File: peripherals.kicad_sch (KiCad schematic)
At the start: 63 parts, among them SW1 USER, SW2 BOOTSEL, SW3 RESET, U2 ATECC608A-MAHDA, U3 W25Q128XXX

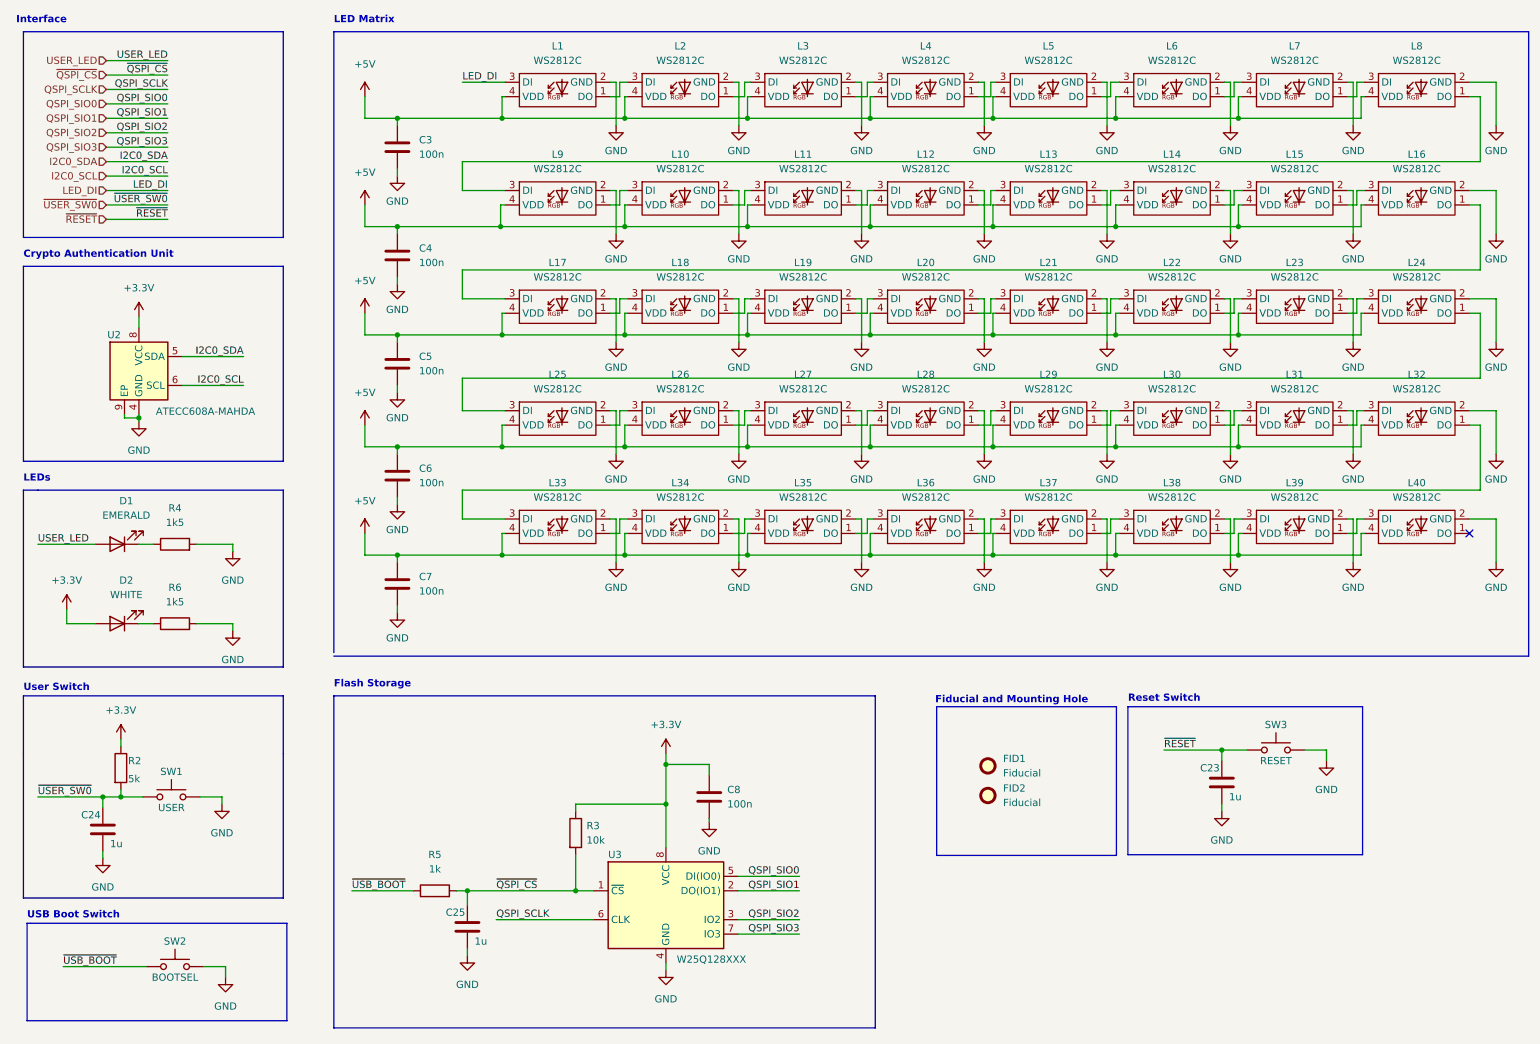
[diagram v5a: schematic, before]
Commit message: Remove trace under usb trace
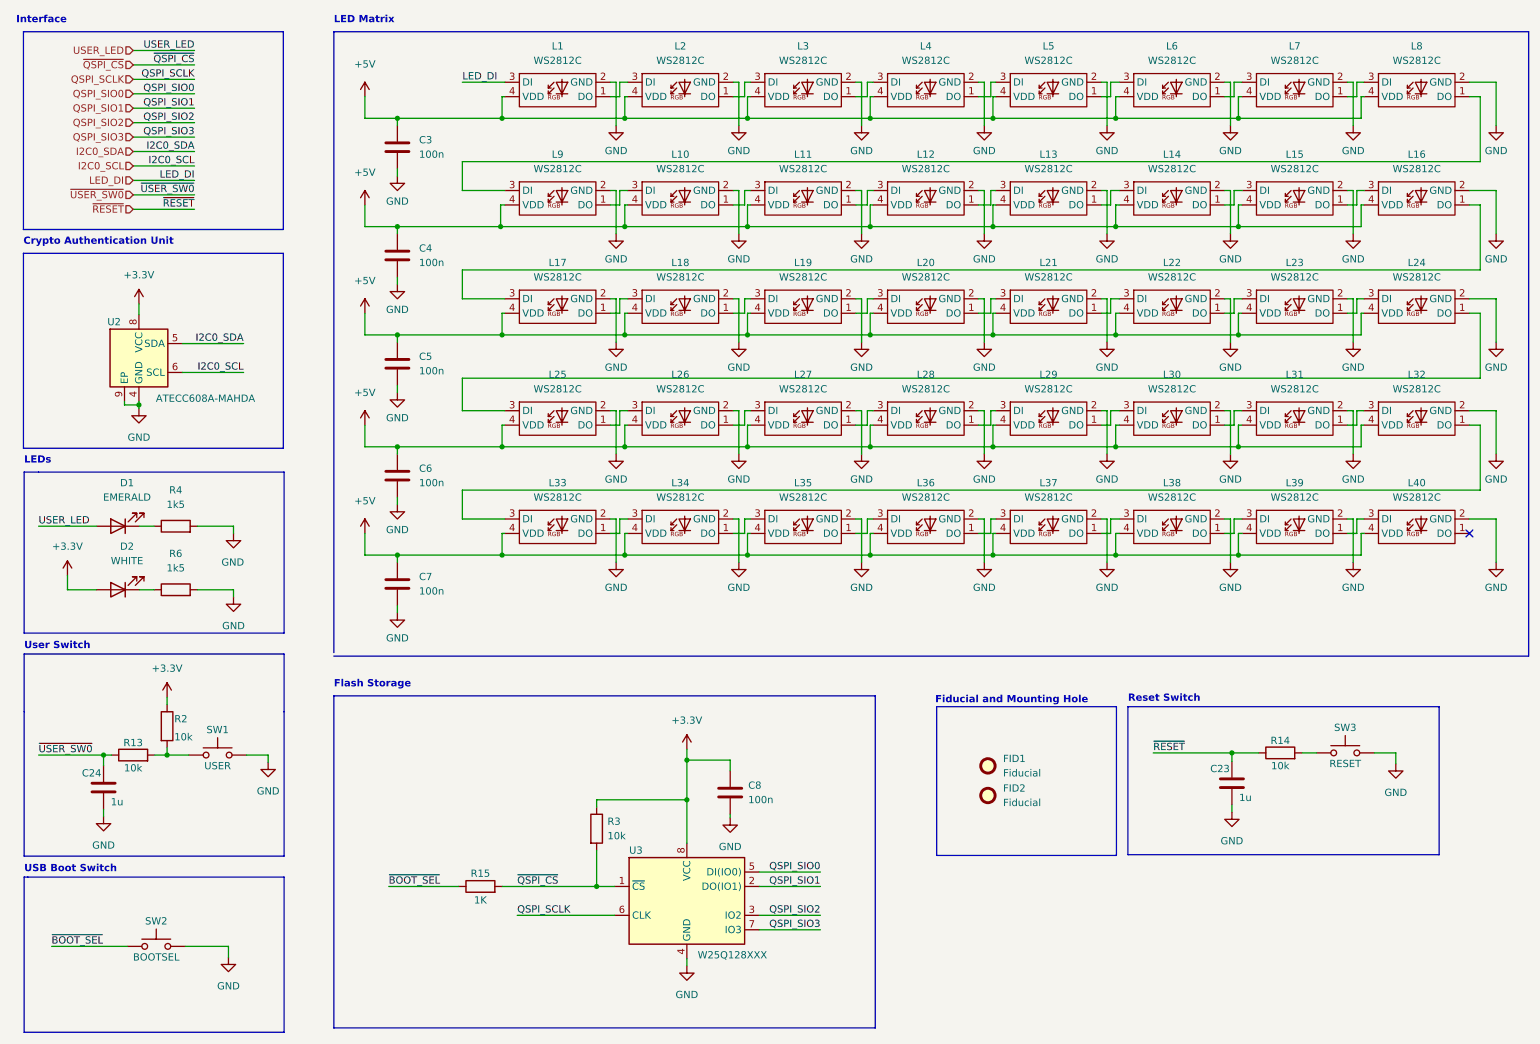
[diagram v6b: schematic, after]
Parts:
- removed C25: 1u, Capacitor_SMD:C_0402_1005Metric, symbol Device:C
- removed R5: 1k, Resistor_SMD:R_0402_1005Metric, symbol Device:R
- added R13, R14: 10k, Resistor_SMD:R_0402_1005Metric, symbol Device:R
- added R15: 1K, Resistor_SMD:R_0402_1005Metric, symbol Device:R
- R2: value 5k -> 10k
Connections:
- net ~{QSPI_CS}: now also R15.2
- net ~{RESET}: now also R14.1; no longer SW3.1
- net ~{USER_SW0}: now also R13.1; no longer R2.2, SW1.1
- net ~{USB_BOOT} renamed ~{BOOT_SEL}
- net ~{BOOT_SEL}: now also R15.1
- new net: R13.2, R2.2, SW1.1
- new net: R14.2, SW3.1
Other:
- moved on the sheet: C23, C24, C8, D1, D2, R2, R3, R4, R6, SW1, SW2, SW3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

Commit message: Production Design V1.0
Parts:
- added R16, R5: 4.7k, Resistor_SMD:R_0402_1005Metric, symbol Device:R
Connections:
- net +3V3: now also R16.1, R5.1
- net I2C0_SCL: now also R16.2
- net I2C0_SDA: now also R5.2
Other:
- moved on the sheet: U2

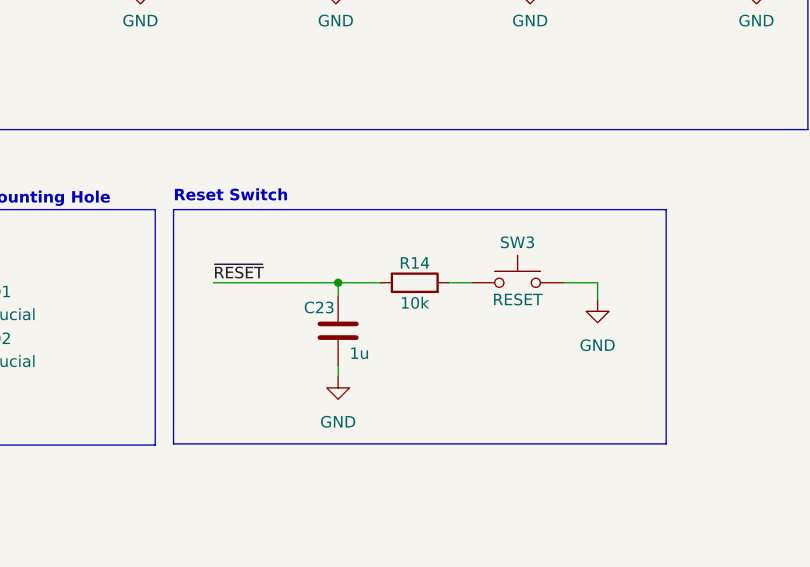
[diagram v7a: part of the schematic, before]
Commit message: Fix issues found on production prototype
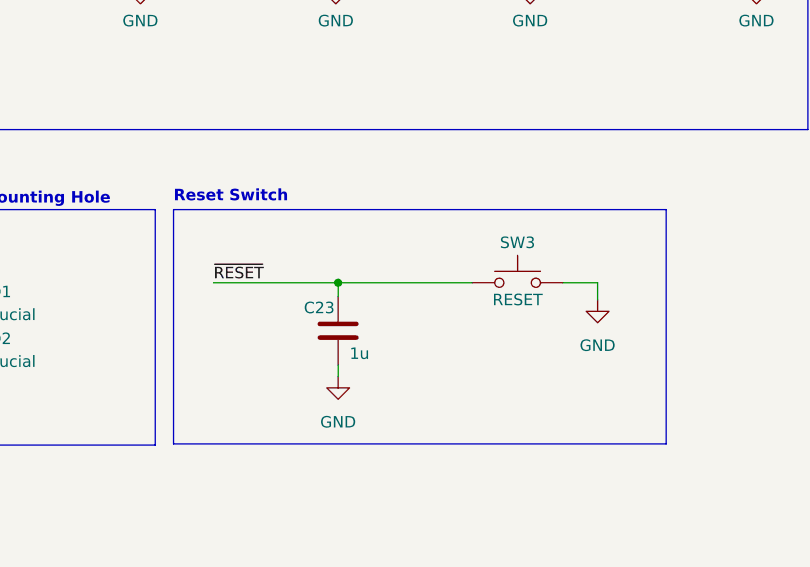
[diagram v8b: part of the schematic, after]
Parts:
- removed R14: 10k, Resistor_SMD:R_0402_1005Metric, symbol Device:R
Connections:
- net ~{RESET}: now also SW3.1
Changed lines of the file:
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@@
   )
   (no_connect (at 270.891 107.315))
-  (wire (pts (xy 229.108 145.923) (xy 233.807 145.923))
+  (wire (pts (xy 229.108 145.923) (xy 243.967 145.923))
     (stroke (width 0) (type default) (color 0 0 0 0))
   )
@@
     (stroke (width 0) (type default) (color 0 0 0 0))
   )
-  (wire (pts (xy 241.427 145.923) (xy 243.967 145.923))
-    (stroke (width 0) (type default) (color 0 0 0 0))
-  )
   (wire (pts (xy 101.219 107.315) (xy 100.711 107.315))
     (stroke (width 0) (type default) (color 0 0 0 0))
@@
     (pin "1")
   )
-  (symbol (lib_id "Device:R") (at 237.617 145.923 90) (unit 1)
-    (in_bom yes) (on_board yes)
-    (property "Reference" "R14" (id 0) (at 237.617 143.764 90))
-    (property "Value" "10k" (id 1) (at 237.617 148.209 90))
-    (property "Footprint" "Resistor_SMD:R_0402_1005Metric" (id 2) (at 237.617 147.701 90)
-      (effects (font (size 1.27 1.27)) hide)
-    )
-    (property "Datasheet" "~" (id 3) (at 237.617 145.923 0)
-      (effects (font (size 1.27 1.27)) hide)
-    )
-    (pin "1")
-    (pin "2")
-  )
   (symbol (lib_id "Switch:SW_Push") (at 249.047 145.923 0) (unit 1)
